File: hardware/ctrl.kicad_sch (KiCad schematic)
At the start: 18 parts, among them J1 Conn_01x06, Q1 BC817W, Q2 BC817W, U1 ESP32-WROOM-32E, U9 ESP32-C3-WROOM-02

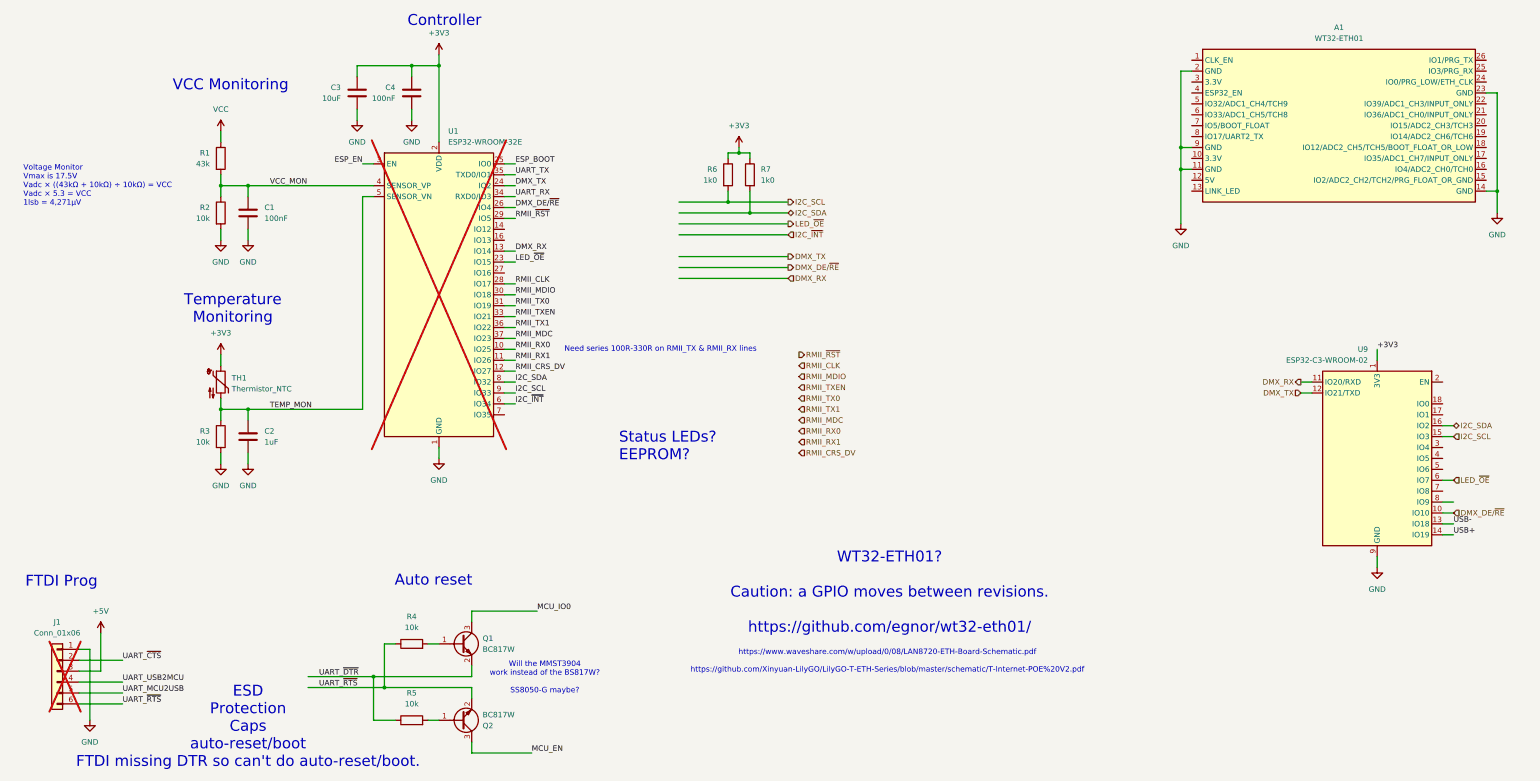
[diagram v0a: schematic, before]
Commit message: adding ESP32 and PSU options
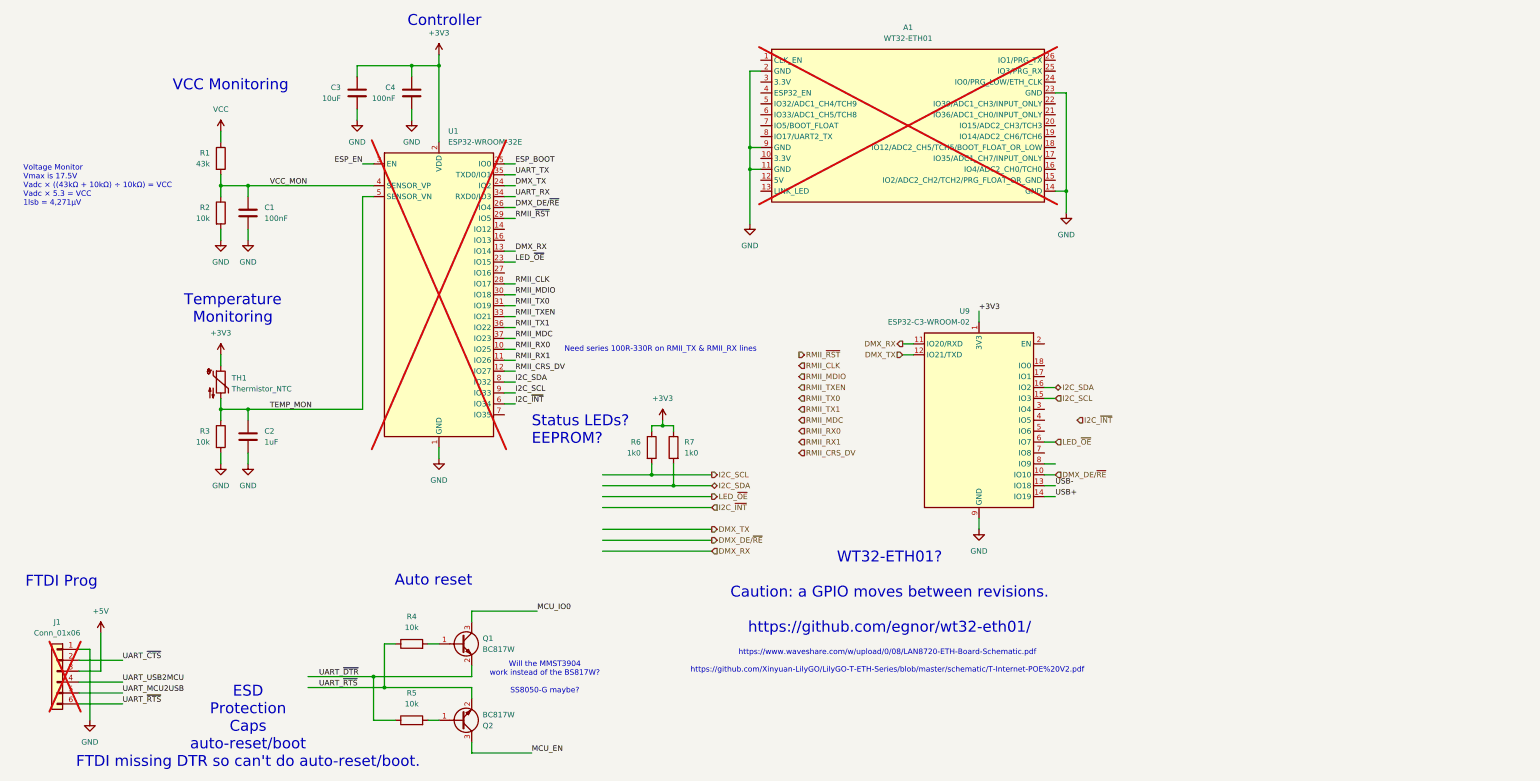
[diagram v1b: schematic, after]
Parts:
- A1: now not fitted
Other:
- moved on the sheet: R6, R7, U9
